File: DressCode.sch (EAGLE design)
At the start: 38 parts, among them M1 MIC9.7MM, M2 MIC6MM, Q1 2N7002, Q2 2N7002, Q3 2N7002, U1 MCP6S21, U2 MCP6S21, U3 MCP6G02, U4 PIC24FV32KA304-I/PT

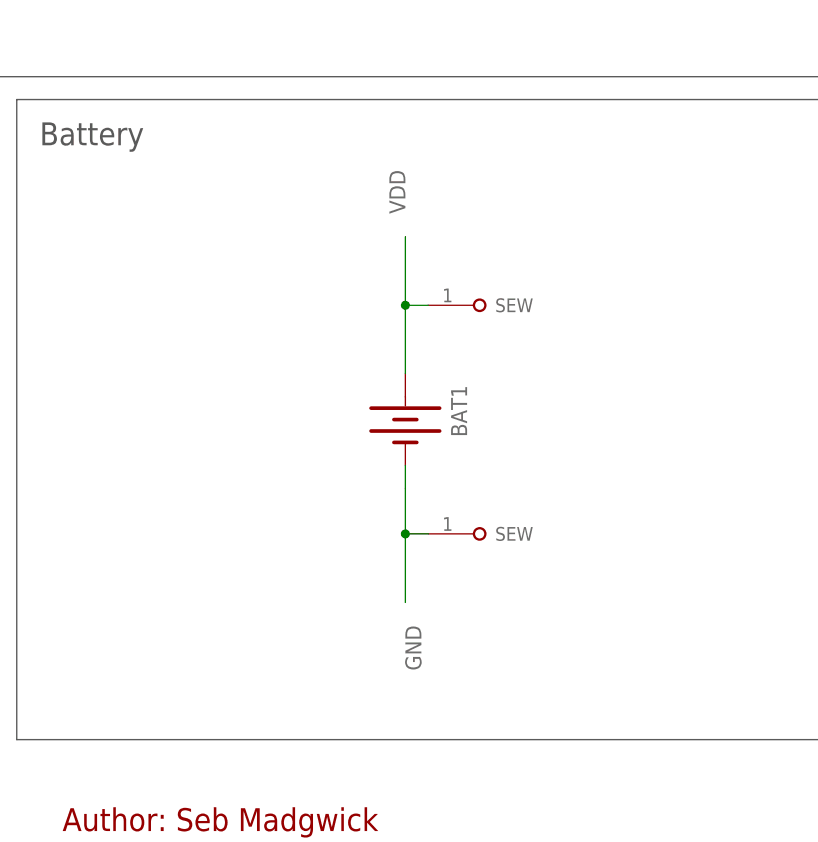
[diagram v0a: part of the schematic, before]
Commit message: JST connector added for LiPo power
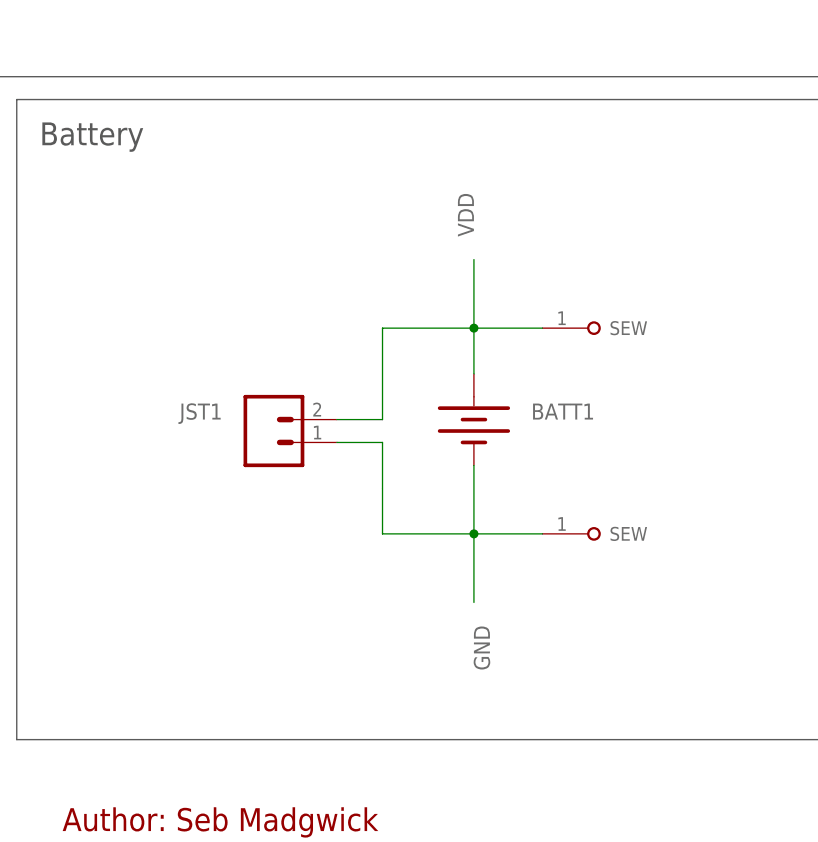
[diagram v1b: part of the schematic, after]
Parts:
- removed BAT1: (no value), SparkFun:BATTERY20PTH
- added BATT1: (no value), SparkFun:BATTERY20PTH
- added JST1: (no value), SparkFun_08_2011:M02-JST-2-PTH-NO_SILK
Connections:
- net GND: now also BATT1.-, JST1.1; no longer BAT1.-
- net VDD: now also BATT1.+, JST1.2; no longer BAT1.+
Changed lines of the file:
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@@
 <part name="R7" library="rcl" deviceset="R-EU_" device="R0805" value="2.2k"/>
 <part name="M2" library="x-io" deviceset="MIC" device="6MM"/>
-<part name="BAT1" library="SparkFun" deviceset="BATTERY" device="20PTH"/>
+<part name="JST1" library="SparkFun_08_2011" deviceset="M02" device="-JST-2-PTH-NO_SILK"/>
+<part name="BATT1" library="SparkFun" deviceset="BATTERY" device="20PTH"/>
 </parts>
 <sheets>
@@
 <instance part="U$5" gate="G$1" x="96.52" y="152.4" rot="R90"/>
 <instance part="U$6" gate="G$1" x="152.4" y="152.4" rot="R90"/>
-<instance part="U$7" gate="G$1" x="340.36" y="48.26" rot="MR180"/>
-<instance part="U$8" gate="G$1" x="340.36" y="73.66" rot="MR180"/>
+<instance part="U$7" gate="G$1" x="353.06" y="48.26" rot="MR180"/>
+<instance part="U$8" gate="G$1" x="353.06" y="71.12" rot="MR180"/>
 <instance part="MCLR" gate="G$1" x="309.88" y="137.16"/>
 <instance part="VDD" gate="G$1" x="320.04" y="137.16"/>
@@
 <attribute name="VALUE" x="33.02" y="38.1" size="1.778" layer="96" rot="MR0"/>
 </instance>
-<instance part="BAT1" gate="G$1" x="332.74" y="60.96" rot="R270"/>
+<instance part="JST1" gate="G$1" x="317.5" y="58.42" smashed="yes">
+<attribute name="VALUE" x="314.96" y="53.34" size="1.778" layer="96"/>
+<attribute name="NAME" x="312.42" y="62.738" size="1.778" layer="95" rot="R180"/>
+</instance>
+<instance part="BATT1" gate="G$1" x="340.36" y="60.96" smashed="yes" rot="R270">
+<attribute name="NAME" x="346.71" y="60.96" size="1.778" layer="95"/>
+<attribute name="VALUE" x="334.01" y="64.77" size="1.778" layer="96" rot="R270"/>
+</instance>
 </instances>
 <busses>
@@
 <segment>
 <pinref part="U$7" gate="G$1" pin="SEW"/>
-<wire x1="335.28" y1="48.26" x2="332.74" y2="48.26" width="0.1524" layer="91"/>
-<label x="332.74" y="38.1" size="1.778" layer="95" rot="R270"/>
-<wire x1="332.74" y1="48.26" x2="332.74" y2="40.64" width="0.1524" layer="91"/>
-<wire x1="332.74" y1="53.34" x2="332.74" y2="48.26" width="0.1524" layer="91"/>
-<junction x="332.74" y="48.26"/>
-<pinref part="BAT1" gate="G$1" pin="-"/>
-<wire x1="332.74" y1="55.88" x2="332.74" y2="53.34" width="0.1524" layer="91"/>
+<wire x1="347.98" y1="48.26" x2="340.36" y2="48.26" width="0.1524" layer="91"/>
+<label x="340.36" y="38.1" size="1.778" layer="95" rot="R270"/>
+<wire x1="340.36" y1="48.26" x2="340.36" y2="40.64" width="0.1524" layer="91"/>
+<wire x1="340.36" y1="55.88" x2="340.36" y2="48.26" width="0.1524" layer="91"/>
+<junction x="340.36" y="48.26"/>
+<pinref part="BATT1" gate="G$1" pin="-"/>
+<pinref part="JST1" gate="G$1" pin="1"/>
+<wire x1="325.12" y1="58.42" x2="330.2" y2="58.42" width="0.1524" layer="91"/>
+<wire x1="330.2" y1="58.42" x2="330.2" y2="53.34" width="0.1524" layer="91"/>
+<wire x1="340.36" y1="48.26" x2="330.2" y2="48.26" width="0.1524" layer="91"/>
+<wire x1="330.2" y1="48.26" x2="330.2" y2="53.34" width="0.1524" layer="91"/>
 </segment>
 <segment>
@@
 <segment>
 <pinref part="U$8" gate="G$1" pin="SEW"/>
-<wire x1="335.28" y1="73.66" x2="332.74" y2="73.66" width="0.1524" layer="91"/>
-<label x="332.74" y="83.82" size="1.778" layer="95" rot="R90"/>
-<pinref part="BAT1" gate="G$1" pin="+"/>
-<wire x1="332.74" y1="73.66" x2="332.74" y2="81.28" width="0.1524" layer="91"/>
-<wire x1="332.74" y1="66.04" x2="332.74" y2="73.66" width="0.1524" layer="91"/>
-<junction x="332.74" y="73.66"/>
-</segment>
-<segment>
+<wire x1="347.98" y1="71.12" x2="340.36" y2="71.12" width="0.1524" layer="91"/>
+<label x="340.36" y="81.28" size="1.778" layer="95" rot="R90"/>
+<wire x1="340.36" y1="71.12" x2="340.36" y2="78.74" width="0.1524" layer="91"/>
+<junction x="340.36" y="71.12"/>
+<pinref part="JST1" gate="G$1" pin="2"/>
+<wire x1="325.12" y1="60.96" x2="330.2" y2="60.96" width="0.1524" layer="91"/>
+<wire x1="330.2" y1="60.96" x2="330.2" y2="71.12" width="0.1524" layer="91"/>
+<wire x1="330.2" y1="71.12" x2="340.36" y2="71.12" width="0.1524" layer="91"/>
+<wire x1="340.36" y1="71.12" x2="340.36" y2="66.04" width="0.1524" layer="91"/>
+<pinref part="BATT1" gate="G$1" pin="+"/>
+</segment>
+<segment>

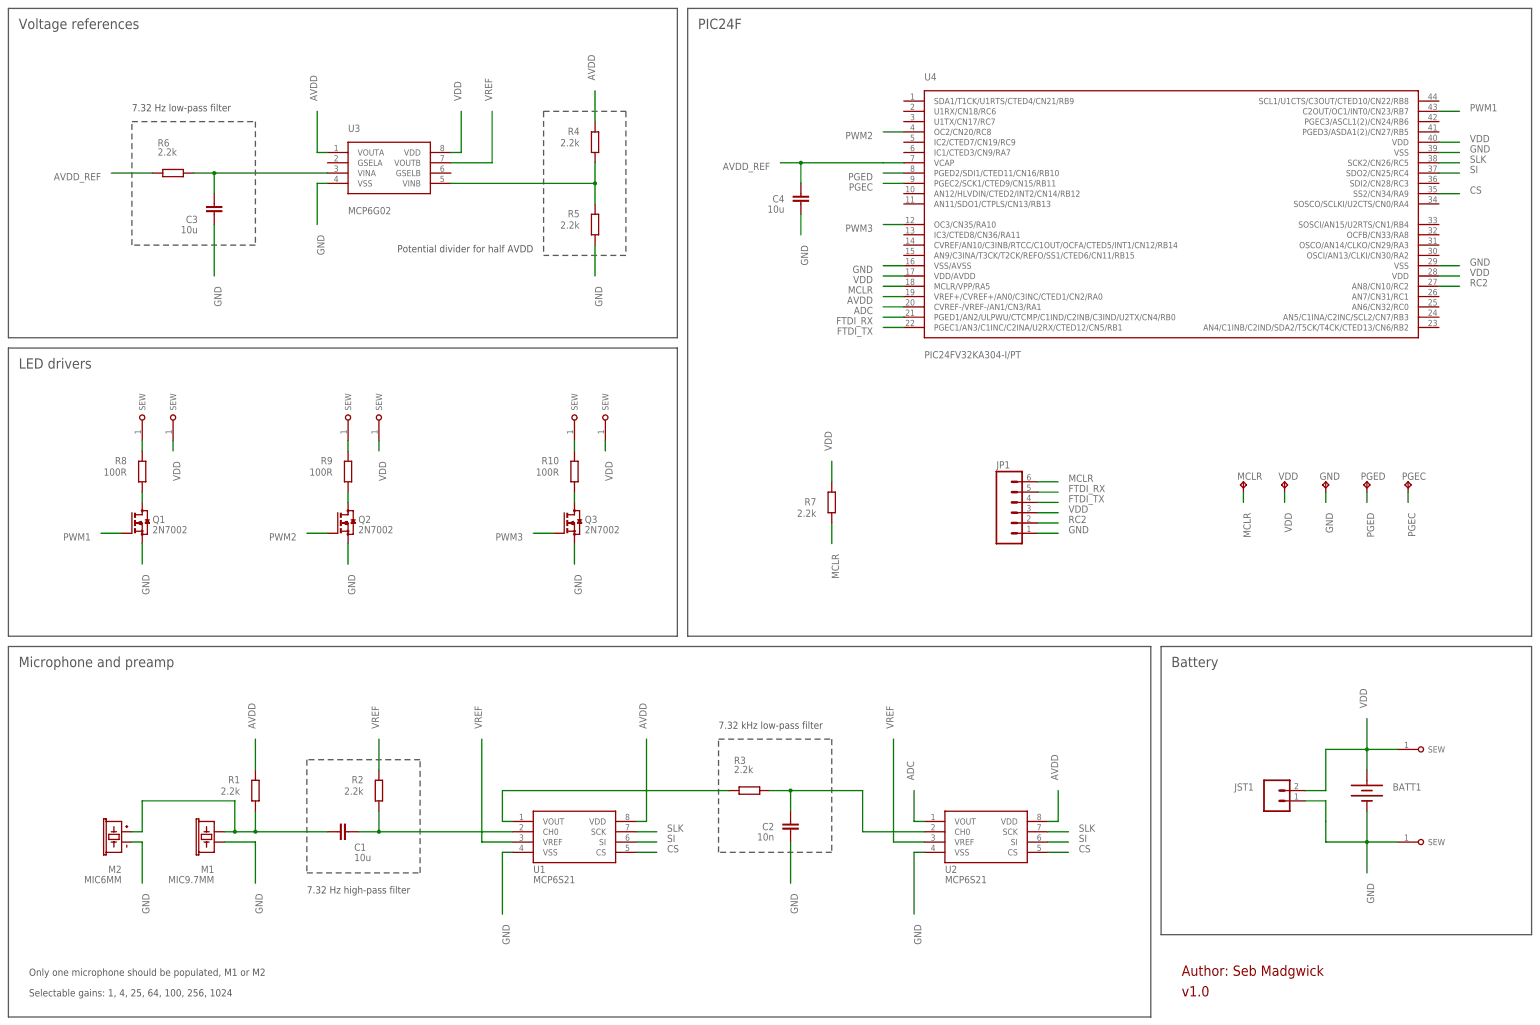
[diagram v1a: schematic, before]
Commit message: design now includes USB charger
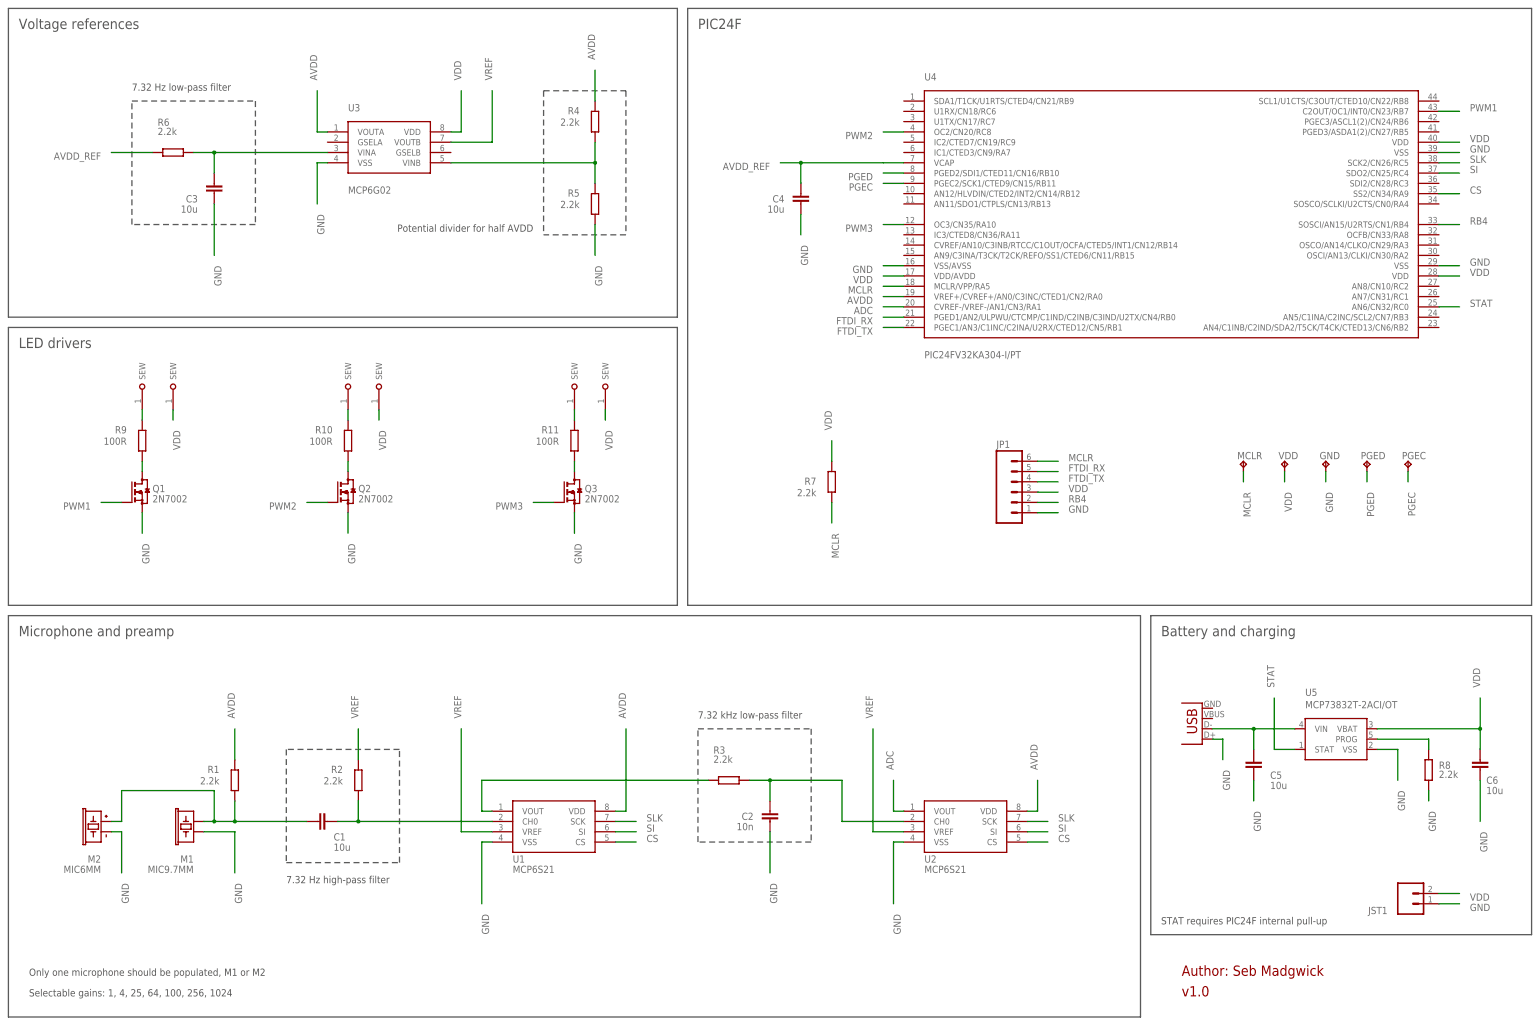
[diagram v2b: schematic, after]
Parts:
- removed BATT1: (no value), SparkFun:BATTERY20PTH
- removed U$1, U$2, U$3: DRESSCODE_SEW_PAD, x-io:DRESSCODE_SEW_PAD
- added C5, C6: 10u, rcl:C-EUC0805
- added R11: 100R, rcl:R-EU_R0805
- added U$10: DRESSCODE_SEW_PADS, x-io:DRESSCODE_SEW_PADS
- added U5: MCP73832T-2ACI/OT, SparkFun_08_2011:MCP73831
- added USB1: USB-MICROB, SparkFun_08_2011:USB-MICROB
- JST1: device SparkFun_08_2011:M02-JST-2-PTH-NO_SILK -> SparkFun_08_2011:M02-JST-2MM-SMT
- R8: value 100R -> 2.2k
- U$4, U$5, U$6: value DRESSCODE_SEW_PAD -> DRESSCODE_SEW_PADC; device x-io:DRESSCODE_SEW_PAD -> x-io:DRESSCODE_SEW_PADC
- U$7, U$8: value DRESSCODE_SEW_PAD -> DRESSCODE_SEW_PADS; device x-io:DRESSCODE_SEW_PAD -> x-io:DRESSCODE_SEW_PADS
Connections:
- removed net RC2: JP1.2, U4.AN8/CN10/RC2
- new net N$15: R8.2, U5.PROG
- new net RB4: JP1.2, U4.SOSCI/AN15/U2RTS/CN1/RB4
- new net STAT: U4.AN6/CN32/RC0, U5.STAT
- new net USB1: C5.2, U5.VIN, USB1.D-
- net GND: now also C5.1, C6.1, R8.1, U5.VSS, USB1.D+; no longer BATT1.-, U$7.SEW
- net N$10: now also R10.1; no longer R9.1
- net N$11: now also R11.1; no longer R10.1
- net N$12: now also R9.2, U$7.SEW; no longer R8.2, U$1.SEW
- net N$13: now also R10.2, U$8.SEW; no longer R9.2, U$2.SEW
- net N$14: now also R11.2, U$10.SEW; no longer R10.2, U$3.SEW
- net N$9: now also R9.1; no longer R8.1
- net VDD: now also C6.2, U5.VBAT; no longer BATT1.+, U$8.SEW
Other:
- note added: "Battery and charging"
- note added: "STAT requires PIC24F internal pull-up"
- note removed: "Battery"
- moved on the sheet: C1, C2, C3, GND, JP1, JST1, M1, M2, MCLR, PGEC, PGED, Q1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
